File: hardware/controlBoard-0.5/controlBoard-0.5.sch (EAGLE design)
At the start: 15 parts, among them J1 AYZ0202

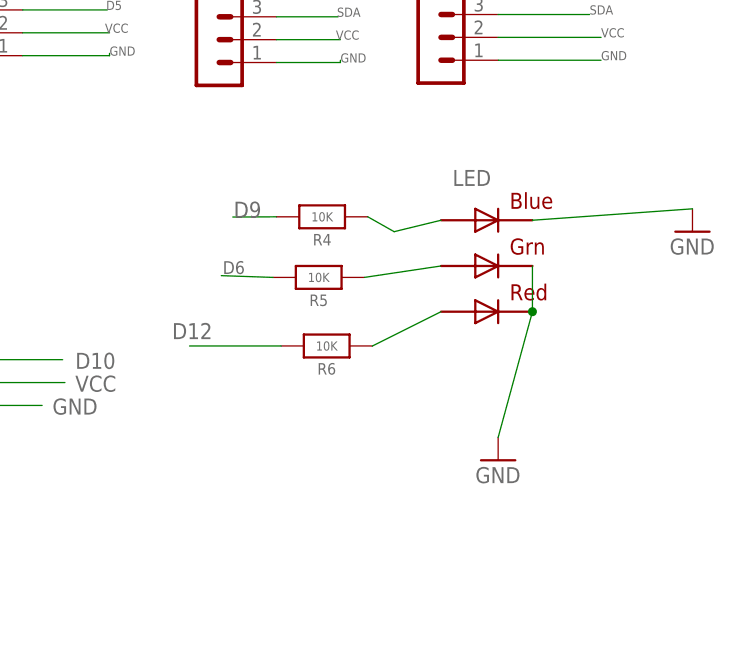
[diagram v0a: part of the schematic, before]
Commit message: control board update
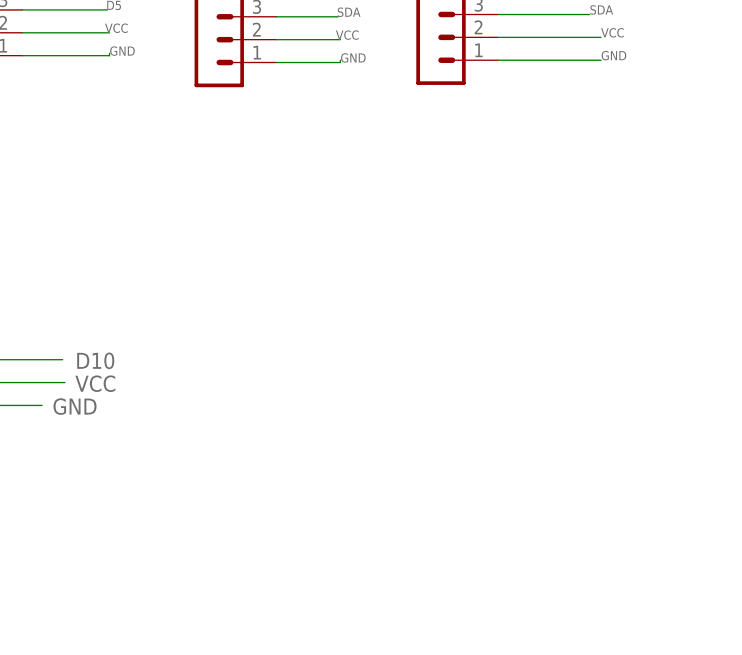
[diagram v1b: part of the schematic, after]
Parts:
- removed LED: RGBLED5050, adafruit:RGBLED5050
- removed R4, R5, R6: 10K, microbuilder:RESISTOR_0603_NOOUT
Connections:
- removed net N$1: LED.RED_A, R6.1
- removed net N$22: LED.BLUE_A, R4.1
- removed net N$23: LED.GREEN_A, R5.1
- net D12: no longer R6.2
- net D6: no longer R5.2
- net D9: no longer R4.2
- net GND: no longer LED.BLUE_C, LED.GREEN_C, LED.RED_C
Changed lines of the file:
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@@
 <?xml version="1.0" encoding="utf-8"?>
 <!DOCTYPE eagle SYSTEM "eagle.dtd">
-<eagle version="6.2">
+<eagle version="8.6.3">
 <drawing>
 <settings>
-<setting alwaysvectorfont="yes"/>
+<setting alwaysvectorfont="no"/>
+<setting keepoldvectorfont="yes"/>
 <setting verticaltext="up"/>
 </settings>
@@
 <part name="R9" library="microbuilder" deviceset="RESISTOR" device="_0603_NOOUT" value="4.7K"/>
 <part name="R10" library="microbuilder" deviceset="RESISTOR" device="_0603_NOOUT" value="4.7K"/>
-<part name="LED" library="adafruit" deviceset="RGBLED" device="5050" value=""/>
-<part name="GND7" library="supply1" deviceset="GND" device=""/>
 <part name="TEMP" library="con-lstb" deviceset="MA04-1" device=""/>
-<part name="R4" library="microbuilder" deviceset="RESISTOR" device="_0603_NOOUT" value="10K"/>
-<part name="R5" library="microbuilder" deviceset="RESISTOR" device="_0603_NOOUT" value="10K"/>
-<part name="R6" library="microbuilder" deviceset="RESISTOR" device="_0603_NOOUT" value="10K"/>
 <part name="COND" library="con-lstb" deviceset="MA04-1" device=""/>
 <part name="TURB" library="pinhead" deviceset="PINHD-1X3" device=""/>
 <part name="LEDSTRAND" library="con-lstb" deviceset="MA04-1" device=""/>
-<part name="GND1" library="supply1" deviceset="GND" device=""/>
 <part name="MS1" library="adafruit" deviceset="FEATHERWING" device=""/>
 <part name="PH" library="con-lstb" deviceset="MA04-1" device="">
@@
 <instance part="R9" gate="G$1" x="98.806" y="136.398" rot="R90"/>
 <instance part="R10" gate="G$1" x="108.966" y="136.398" rot="R90"/>
-<instance part="LED" gate="G$1" x="203.2" y="67.31" smashed="yes">
-<attribute name="NAME" x="199.39" y="76.2" size="1.778" layer="95"/>
-</instance>
-<instance part="GND7" gate="1" x="204.47" y="45.72"/>
 <instance part="TEMP" gate="1" x="172.212" y="94.996"/>
-<instance part="R4" gate="G$1" x="184.912" y="72.771" rot="R180"/>
-<instance part="R5" gate="G$1" x="184.531" y="66.04" rot="R180"/>
-<instance part="R6" gate="G$1" x="185.42" y="58.42" rot="R180"/>
 <instance part="COND" gate="1" x="144.018" y="95.758"/>
 <instance part="TURB" gate="A" x="140.335" y="54.356" rot="R180"/>
 <instance part="LEDSTRAND" gate="1" x="138.43" y="124.46"/>
-<instance part="GND1" gate="1" x="226.06" y="71.12"/>
 <instance part="MS1" gate="G$1" x="76.2" y="48.26"/>
 <instance part="PH" gate="1" x="196.85" y="95.25"/>
@@
 <net name="GND" class="0">
 <segment>
-<pinref part="GND7" gate="1" pin="GND"/>
-<pinref part="LED" gate="G$1" pin="GREEN_C"/>
-<pinref part="LED" gate="G$1" pin="RED_C"/>
-<wire x1="208.28" y1="67.31" x2="208.28" y2="62.23" width="0.1524" layer="91"/>
-<wire x1="208.28" y1="62.23" x2="204.47" y2="48.26" width="0.1524" layer="91"/>
-<junction x="208.28" y="62.23"/>
-</segment>
-<segment>
 <pinref part="J1" gate="G$1" pin="5"/>
 <wire x1="200.66" y1="124.46" x2="192.786" y2="124.46" width="0.1524" layer="91"/>
@@
 <pinref part="TURB" gate="A" pin="1"/>
 <label x="154.94" y="50.8" size="1.778" layer="95"/>
-</segment>
-<segment>
-<pinref part="LED" gate="G$1" pin="BLUE_C"/>
-<wire x1="208.28" y1="72.39" x2="226.06" y2="73.66" width="0.1524" layer="91"/>
-<pinref part="GND1" gate="1" pin="GND"/>
 </segment>
 <segment>
@@
 </segment>
 </net>
-<net name="N$22" class="0">
-<segment>
-<pinref part="LED" gate="G$1" pin="BLUE_A"/>
-<wire x1="198.12" y1="72.39" x2="192.913" y2="71.12" width="0.1524" layer="91"/>
-<pinref part="R4" gate="G$1" pin="1"/>
-<wire x1="192.913" y1="71.12" x2="189.992" y2="72.771" width="0.1524" layer="91"/>
-</segment>
-</net>
-<net name="N$23" class="0">
-<segment>
-<pinref part="R5" gate="G$1" pin="1"/>
-<wire x1="198.12" y1="67.31" x2="189.611" y2="66.04" width="0.1524" layer="91"/>
-<pinref part="LED" gate="G$1" pin="GREEN_A"/>
-</segment>
-</net>
 <net name="D11" class="0">
 <segment>
@@
 <net name="D9" class="0">
 <segment>
-<label x="175.0822" y="72.6694" size="1.778" layer="95"/>
-<wire x1="179.832" y1="72.771" x2="174.9806" y2="72.7456" width="0.1524" layer="91"/>
-<pinref part="R4" gate="G$1" pin="2"/>
-</segment>
-<segment>
 <label x="109.22" y="88.392" size="1.016" layer="95"/>
 <wire x1="109.22" y1="106.68" x2="109.26" y2="88.2994" width="0.1524" layer="91"/>
@@
 </segment>
 </net>
-<net name="N$1" class="0">
-<segment>
-<pinref part="R6" gate="G$1" pin="1"/>
-<pinref part="LED" gate="G$1" pin="RED_A"/>
-<wire x1="198.12" y1="62.23" x2="190.5" y2="58.42" width="0.1524" layer="91"/>
-</segment>
-</net>
 <net name="VBAT" class="0">
 <segment>
@@
 <net name="D6" class="0">
 <segment>
-<label x="173.863" y="66.421" size="1.4224" layer="95"/>
-<wire x1="179.451" y1="66.04" x2="173.705940625" y2="66.233984375" width="0.1524" layer="91"/>
-<pinref part="R5" gate="G$1" pin="2"/>
-</segment>
-<segment>
 <pinref part="MS1" gate="G$1" pin="GPIO6"/>
 <wire x1="111.76" y1="106.68" x2="111.76" y2="91.44" width="0.1524" layer="91"/>
@@
 <net name="D12" class="0">
 <segment>
-<wire x1="180.34" y1="58.42" x2="170.18" y2="58.42" width="0.1524" layer="91"/>
-<pinref part="R6" gate="G$1" pin="2"/>
-<label x="172.72" y="60.96" size="1.778" layer="95" rot="R180"/>
-</segment>
-<segment>
 <pinref part="MS1" gate="G$1" pin="GPIO12"/>
